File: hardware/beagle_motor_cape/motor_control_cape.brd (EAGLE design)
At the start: 54.6 x 71.8 mm, 26 parts, among them IC1 MCP4911SN, IC2 MCP4911SN

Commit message: Continue work on BeagleBone Black cape
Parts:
- removed IC3: (no value), INA219:SO08
- added C4, C5, C6: 0.1uF, resistor:C0603
- added D1, D2, D3, D4: 3.3V, diode:SOT23
- added LED1, LED2: (no value), adafruit:CHIPLED_0603
- added Q7, Q8: (no value), adafruit:SOT23
- added R14, R15: 1k, rcl:R0603
- added R16, R18: 2k, rcl:R0603
- added R17: 11.3k, rcl:R0603
- added U1, U2: BTS50055-1TMA, BTS50055-1TMA:TO127P1385X450-8N-V
- C3: value 1uF -> 0.1uF
- R10: value DNP -> 0
- R11: value DNP -> 681
- R12: value 4.7k -> 1k
- R13: value 4.7k -> 11.3k
- R7: value CSS2H-2512R-1L00F -> 681; device resistor:R6332 -> rcl:R0603
- R8: value 1k -> 0
- moved R7 117.2 mm to (-50.8, -228.6)
- moved R8 109.2 mm to (-45.7, -228.6)
- moved R9 104.1 mm to (-41.9, -228.6)
- moved R13 93.3 mm to (-67.3, -234.9)
- moved R12 89.8 mm to (-55.9, -228.6)
- moved C3 81.0 mm to (-62.2, -228.6)
- moved R10 35.9 mm to (-62.2, -160.0)
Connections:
- net MOTOR0_SENSE renamed MOTOR0_TACH
- net MOTOR1_SENSE renamed MOTOR1_TACH
- removed net BATT0_IN: IC3.8, R7.2
- removed net BATT0_OUT: IC3.7, R7.1
- removed net I2C_SCL: IC3.4, R13.1
- removed net I2C_SDA: IC3.3, R12.1
- removed net VS: IC3.5
- new net MOTOR0_EN: Q7.1, R14.2, R15.2
- new net MOTOR0_SENSE_AD: R10.2
- new net MOTOR1_EN: Q8.1, R12.2, R9.2
- new net MOTOR1_SENSE_AD: R8.2
- new net N$4: C4.1, D1.3, R10.1, R11.2, U1.5
- new net N$5: Q7.3, U1.3
- new net N$6: LED1.A, R15.1
- new net VCC: R13.2, U1.4, U1.8
- new net VCC_SENSE_AD: C5.1, D3.3, R13.1, R16.1
- new net VDD: R17.2, U2.4, U2.8
- new net VDD_SENSE_AD: C6.1, D4.3, R17.1, R18.1
- net +3V3: no longer R12.2, R13.2, R8.2, R9.2
- net GND: now also C4.2, C5.2, C6.2, D1.1, D2.1, D3.1, D4.1, LED1.C, LED2.C, Q7.2, Q8.2, R14.1, R16.2, R18.2, R7.1, R9.1, U1.1, U1.2, U1.6, U1.7, U2.1, U2.2, U2.6, U2.7; no longer IC3.6, R10.1
- net N$1: now also C3.1, D2.3, R7.2, R8.1, U2.5; no longer IC3.1, R10.2, R9.1
- net N$2: now also Q8.3, U2.3; no longer IC3.2, R11.2, R8.1
- net N$3: now also LED2.A, R12.1; no longer C3.1

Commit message: Finish motor control cape schematic
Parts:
- added C7, C8: 4.7uF, resistor:C0805
- added C9: 0.1uF, resistor:C0603
- added D5: 1.8V, diode:SOT23
- added IC3: 7805TV, linear:TO220V
- added LED3, LED4, LED5, LED6, LED7: (no value), adafruit:CHIPLED_0603
- added PAD1, PAD13, PAD14, PAD2, PAD3, PAD4: WIREPADSMD2,54-5,08, wirepad:SMD2,54-5,08
- added PAD10, PAD11, PAD12, PAD5, PAD6, PAD7, PAD8, PAD9: WIREPAD2,54/1,0, wirepad:2,54/1,0
- added R19, R25: 1k, rcl:R0603
- added R20, R21, R22, R23: 10k, rcl:R0603
- added R24: 11.3k, rcl:R0603
- added TP1, TP2, TP3, TP4, TP5, TP6: TPB1,27, testpad:B1,27
- D1, D2, D3, D4: value 3.3V -> 1.8V
- R11, R7: value 681 -> 383
- R12, R15: value 1k -> 10k
- R16, R18: value 2k -> 1k
- moved D4 373.8 mm to (120.7, 64.8)
- moved R18 373.8 mm to (119.4, 48.3)
- moved C3 373.8 mm to (124.5, 95.2)
- moved C5 373.8 mm to (120.7, 71.1)
- moved C6 373.8 mm to (120.7, 58.4)
- moved D3 373.8 mm to (120.7, 77.5)
- moved LED2 373.8 mm to (119.4, 94.0)
- moved R12 373.8 mm to (130.8, 95.2)
- moved R13 373.8 mm to (119.4, 88.9)
- moved R16 373.8 mm to (119.4, 83.8)
- moved R17 373.8 mm to (119.4, 53.3)
- moved R7 373.8 mm to (135.9, 95.2)
- moved R8 373.8 mm to (141.0, 95.2)
- moved R9 373.8 mm to (144.8, 95.2)
- moved C4 291.4 mm to (133.3, 62.2)
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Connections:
- removed net AIN0: U$1.85
- removed net GPIO_XX: Q5.3, R5.1
- removed net GPIO_YY: Q6.3, R6.1
- removed net VDD_3V3EXP: U$1.49, U$1.50
- removed net VDD_5V: U$1.51, U$1.52
- new net MOTOR0_HS: PAD2.1, U1.1, U1.2, U1.6, U1.7
- new net MOTOR0_TACH_FILT: Q5.3, R5.1, U$1.15
- new net MOTOR1_HS: PAD4.1, U2.1, U2.2, U2.6, U2.7
- new net MOTOR1_TACH_FILT: Q6.3, R6.1, U$1.16
- new net N$10: LED6.A, R22.1
- new net N$11: LED7.A, R23.1
- new net N$7: LED3.A, R19.1
- new net N$8: LED4.A, R20.1
- new net N$9: LED5.A, R21.1
- new net SYS_5V: U$1.53
- new net VBATT: C7.1, IC3.1, PAD13.1, R24.2
- new net VBATT_SENSE_AD: C9.1, D5.3, R24.1, R25.1, U$1.79
- net +3V3: now also U$1.49, U$1.50
- net +5V: now also C8.1, IC3.3, R19.2, U$1.51, U$1.52; no longer U$1.53, U$1.54
- net GND: now also C7.2, C8.2, C9.2, D5.1, IC3.2, LED3.C, LED4.C, LED5.C, LED6.C, LED7.C, PAD14.1, R25.2; no longer U1.1, U1.2, U1.6, U1.7, U2.1, U2.2, U2.6, U2.7
- net GPIO_48: now also R22.2
- net GPIO_50: now also R21.2
- net GPIO_51: now also R23.2
- net GPIO_60: now also R20.2
- net MOTOR0_FWD: now also PAD6.1
- net MOTOR0_REV: now also PAD7.1
- net MOTOR0_SENSE_AD: now also U$1.86
- net MOTOR0_TACH: now also PAD12.1
- net MOTOR0_TRIGGER: now also PAD5.1
- net MOTOR1_FWD: now also PAD9.1
- net MOTOR1_REV: now also PAD10.1
- net MOTOR1_SENSE_AD: now also U$1.84
- net MOTOR1_TACH: now also PAD11.1
- net MOTOR1_TRIGGER: now also PAD8.1
- net SPI0_CS: now also TP3.TP
- net SPI0_MOSI: now also TP1.TP
- net SPI0_SCLK: now also TP2.TP
- net SPI1_CS: now also TP6.TP
- net SPI1_MOSI: now also TP4.TP
- net SPI1_SCLK: now also TP5.TP
- net VCC: now also PAD1.1
- net VCC_SENSE_AD: now also U$1.85
- net VDD: now also PAD3.1
- net VDD_SENSE_AD: now also U$1.83

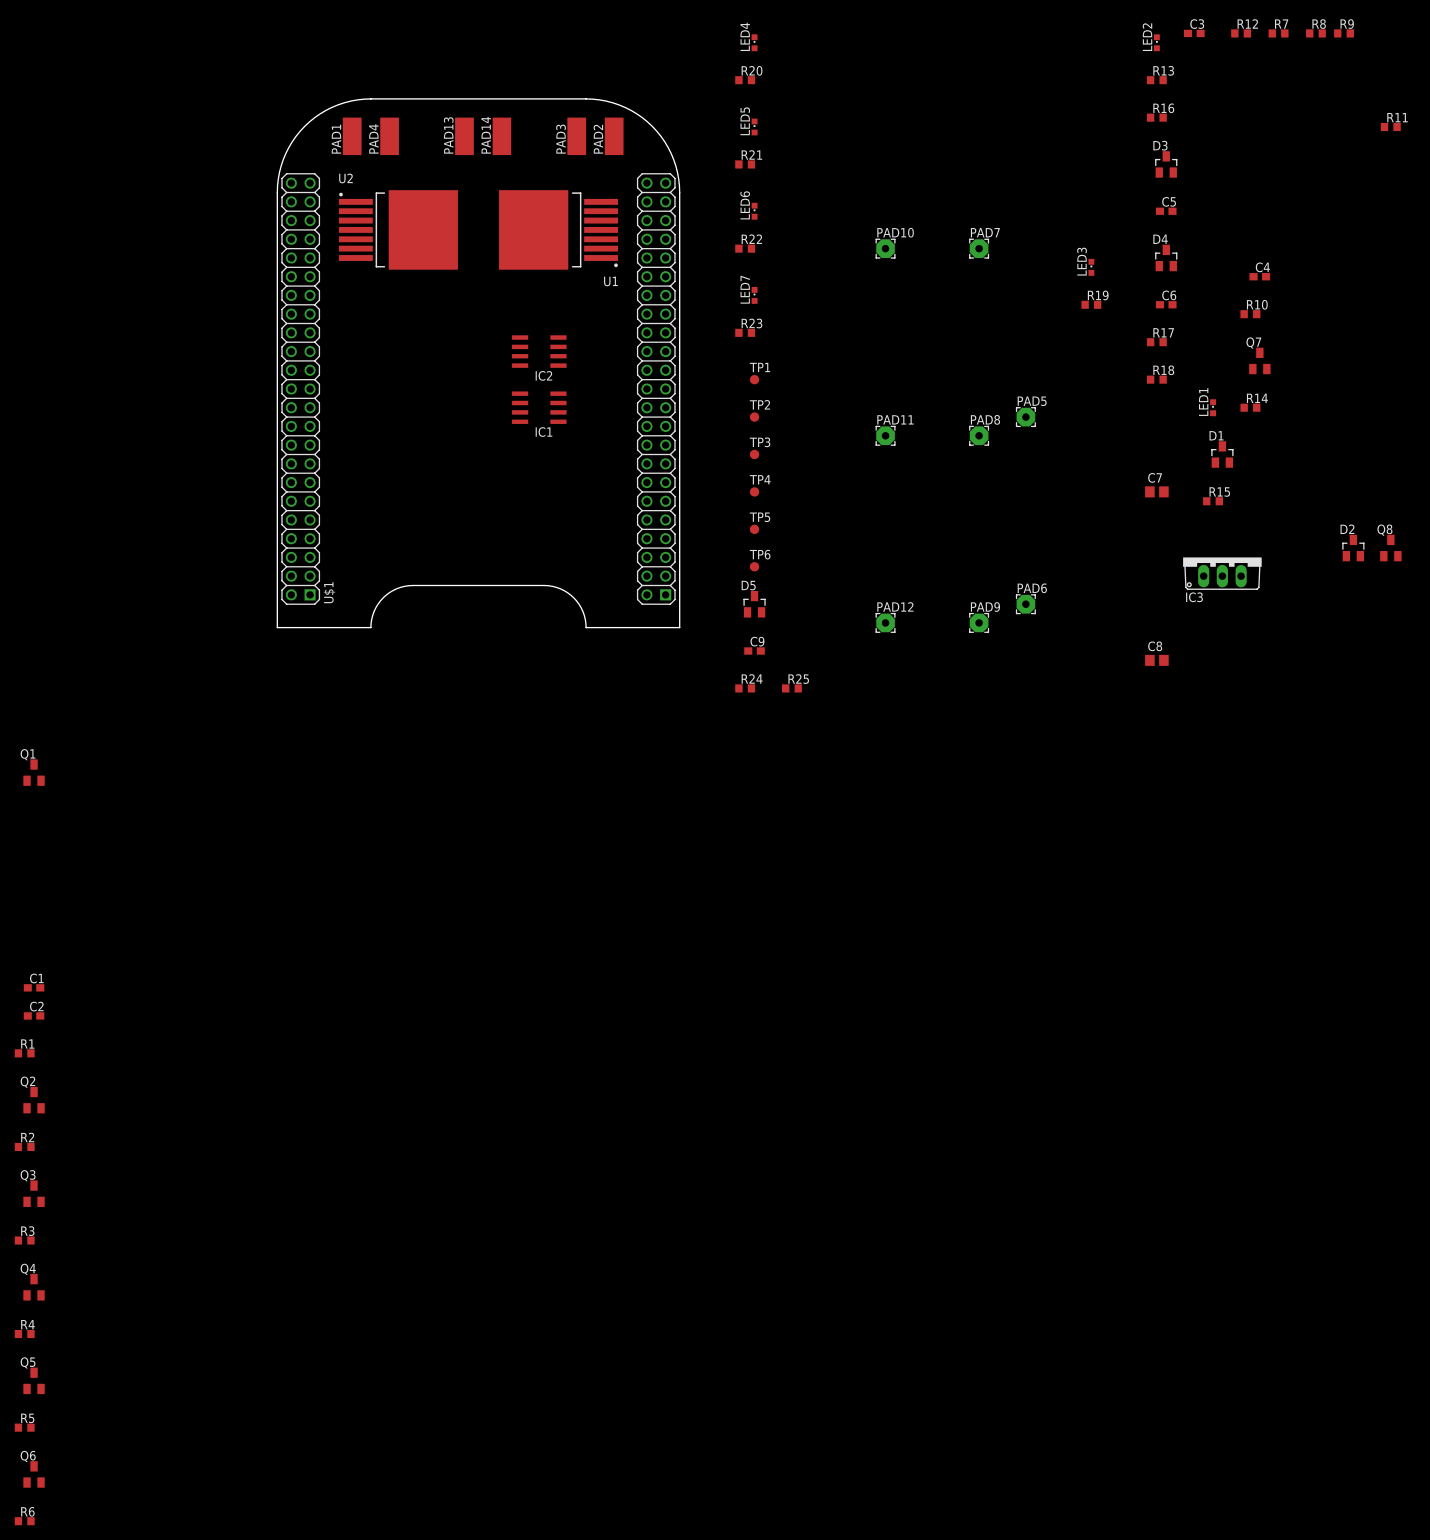
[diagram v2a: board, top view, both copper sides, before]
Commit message: More layout on motor control cape
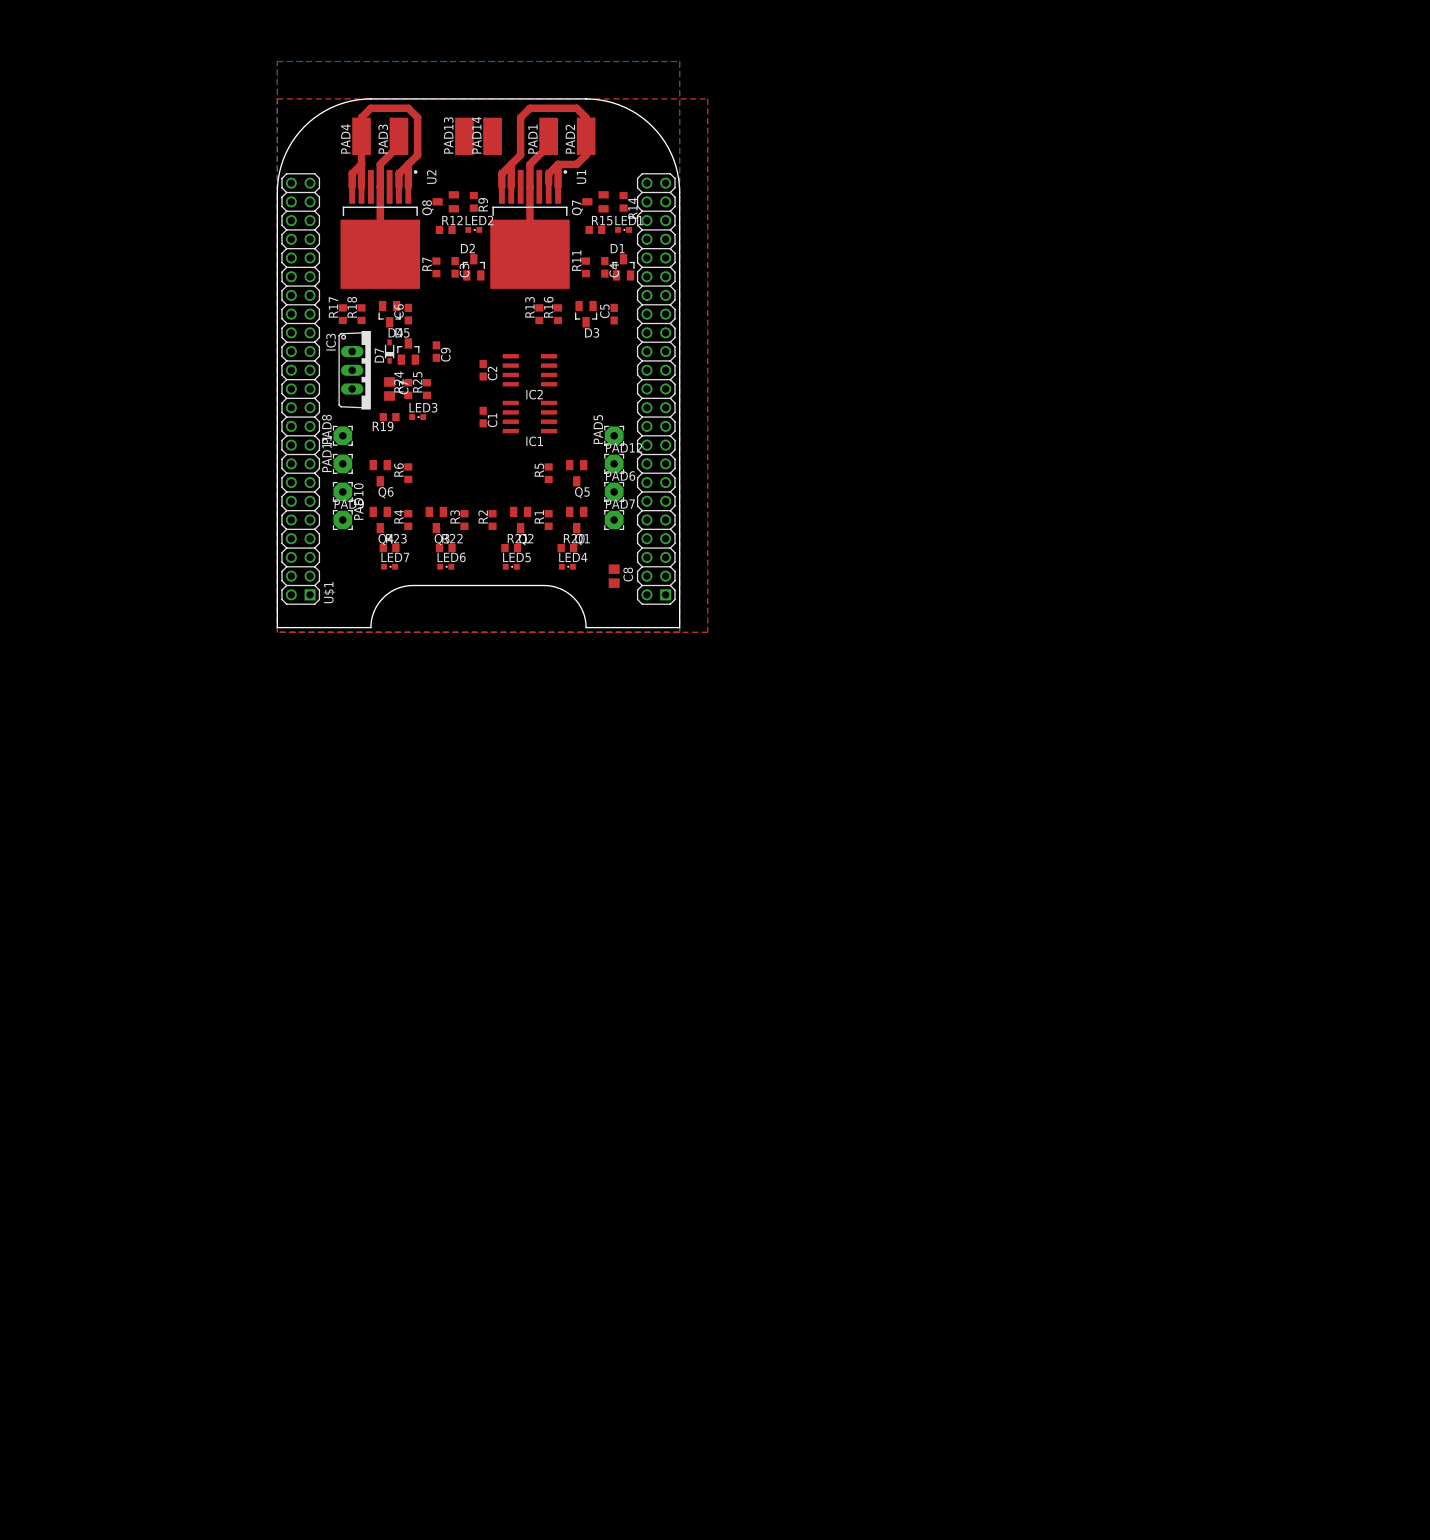
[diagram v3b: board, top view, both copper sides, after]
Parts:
- removed R10, R8: 0, rcl:R0603
- removed TP1, TP2, TP3, TP4, TP5, TP6: TPB1,27, testpad:B1,27
- added D7: BAT60J, diode:SOD323_ST
- moved R6 151.5 mm to (17.8, 35.6), turned to 90 degrees
- moved R5 147.8 mm to (36.8, 35.6), turned to 90 degrees
- moved Q6 143.8 mm to (14.0, 35.6), turned to 180 degrees
- moved Q5 143.5 mm to (40.6, 35.6), turned to 180 degrees
- moved Q8 136.6 mm to (22.9, 72.4), turned to 90 degrees
- moved D2 125.3 mm to (26.7, 63.5)
- moved R4 122.1 mm to (17.8, 29.2), turned to 90 degrees
- moved R9 120.3 mm to (26.7, 72.4), turned to 270 degrees
- moved R7 118.6 mm to (21.6, 63.5), turned to 90 degrees
- moved IC3 118.3 mm to (12.7, 49.5), turned to 270 degrees
- moved R3 114.6 mm to (25.4, 29.2), turned to 90 degrees
- moved Q4 114.3 mm to (14.0, 29.2), turned to 180 degrees
- moved R12 111.2 mm to (22.9, 68.6)
- moved R11 110.9 mm to (41.9, 63.5), turned to 90 degrees
- moved R17 110.6 mm to (8.89, 57.1), turned to 90 degrees
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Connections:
- removed net N$1: C3.1, D2.3, R7.2, R8.1, U2.5
- removed net N$4: C4.1, D1.3, R10.1, R11.2, U1.5
- new net VBATT_FILT: C7.1, D7.C, IC3.1, R24.2
- net MOTOR0_EN: now also U$1.88
- net MOTOR0_SENSE_AD: now also C4.1, D1.3, R11.2, U1.5; no longer R10.2
- net MOTOR1_EN: now also U$1.87
- net MOTOR1_SENSE_AD: now also C3.1, D2.3, R7.2, U2.5; no longer R8.2
- net SPI0_CS: no longer TP3.TP
- net SPI0_MOSI: no longer TP1.TP
- net SPI0_SCLK: no longer TP2.TP
- net SPI1_CS: no longer TP6.TP
- net SPI1_MOSI: no longer TP4.TP
- net SPI1_SCLK: no longer TP5.TP
- net VBATT: now also D7.A; no longer C7.1, IC3.1, R24.2
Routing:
- net MOTOR0_HS: track 0.00 -> 39.0 mm
- net MOTOR1_HS: track 0.00 -> 35.1 mm
- net VDD: track 0.00 -> 17.6 mm
- net VCC: track 0.00 -> 17.6 mm
- added copper zone on layer 1, net GND
- added copper zone on layer 16, net GND

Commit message: Finish laying out motor control cape
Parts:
- moved PAD13 27.3 mm to (11.4, 57.8), turned to 90 degrees
- moved PAD14 25.9 mm to (18.4, 57.8), turned to 90 degrees
- moved R14 16.1 mm to (31.8, 67.3)
- moved C3 15.7 mm to (8.89, 67.3)
- moved Q7 14.9 mm to (29.2, 67.3), turned to 0 degrees
- moved D2 13.3 mm to (14.0, 67.3)
- moved PAD4 11.7 mm to (22.9, 83.8), turned to 90 degrees
- moved PAD1 11.5 mm to (48.3, 80.0)
- moved R7 10.9 mm to (11.4, 67.3)
- moved R13 10.6 mm to (45.7, 60.3)
- moved PAD2 10.5 mm to (31.8, 83.8), turned to 90 degrees
- moved LED1 10.2 mm to (36.8, 67.3), turned to 180 degrees
- moved PAD3 10.2 mm to (6.35, 80.0)
- moved LED2 10.2 mm to (16.5, 67.3), turned to 180 degrees
- moved R15 8.98 mm to (34.3, 67.3), turned to 270 degrees
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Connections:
- new net N$1: U1.4
- new net VBB: U2.4
- net VCC: no longer U1.4
- net VCC_SENSE_AD: now also U$1.83; no longer U$1.85
- net VDD: no longer U2.4
- net VDD_SENSE_AD: now also U$1.85; no longer U$1.83
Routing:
- net +3V3: track 0.00 -> 130.0 mm, vias 0 -> 4
- net +5V: track 0.00 -> 71.8 mm, vias 0 -> 1
- net MOTOR1_SENSE_AD: track 0.00 -> 59.3 mm
- net VDD_SENSE_AD: track 0.00 -> 49.0 mm
- net VBATT_SENSE_AD: track 0.00 -> 48.5 mm
- net GPIO_51: track 0.00 -> 47.7 mm, vias 0 -> 2
- net MOTOR1_EN: track 0.00 -> 41.5 mm, vias 0 -> 1
- net GPIO_48: track 0.00 -> 38.7 mm, vias 0 -> 1
- net MOTOR0_TACH_FILT: track 0.00 -> 38.1 mm
- net GPIO_50: track 0.00 -> 32.5 mm, vias 0 -> 1
- net MOTOR1_TRIGGER: track 0.00 -> 31.4 mm
- net MOTOR0_SENSE_AD: track 0.00 -> 31.1 mm
- net MOTOR0_EN: track 0.00 -> 29.6 mm
- net MOTOR1_FWD: track 0.00 -> 22.4 mm
- net GPIO_60: track 0.00 -> 22.2 mm
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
